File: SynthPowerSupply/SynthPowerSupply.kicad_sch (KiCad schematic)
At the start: 24 parts, among them J1 Barrel_Jack_Switch, U1 LM7812_TO220, U2 LM7912_TO220, U5 LM7805_TO220

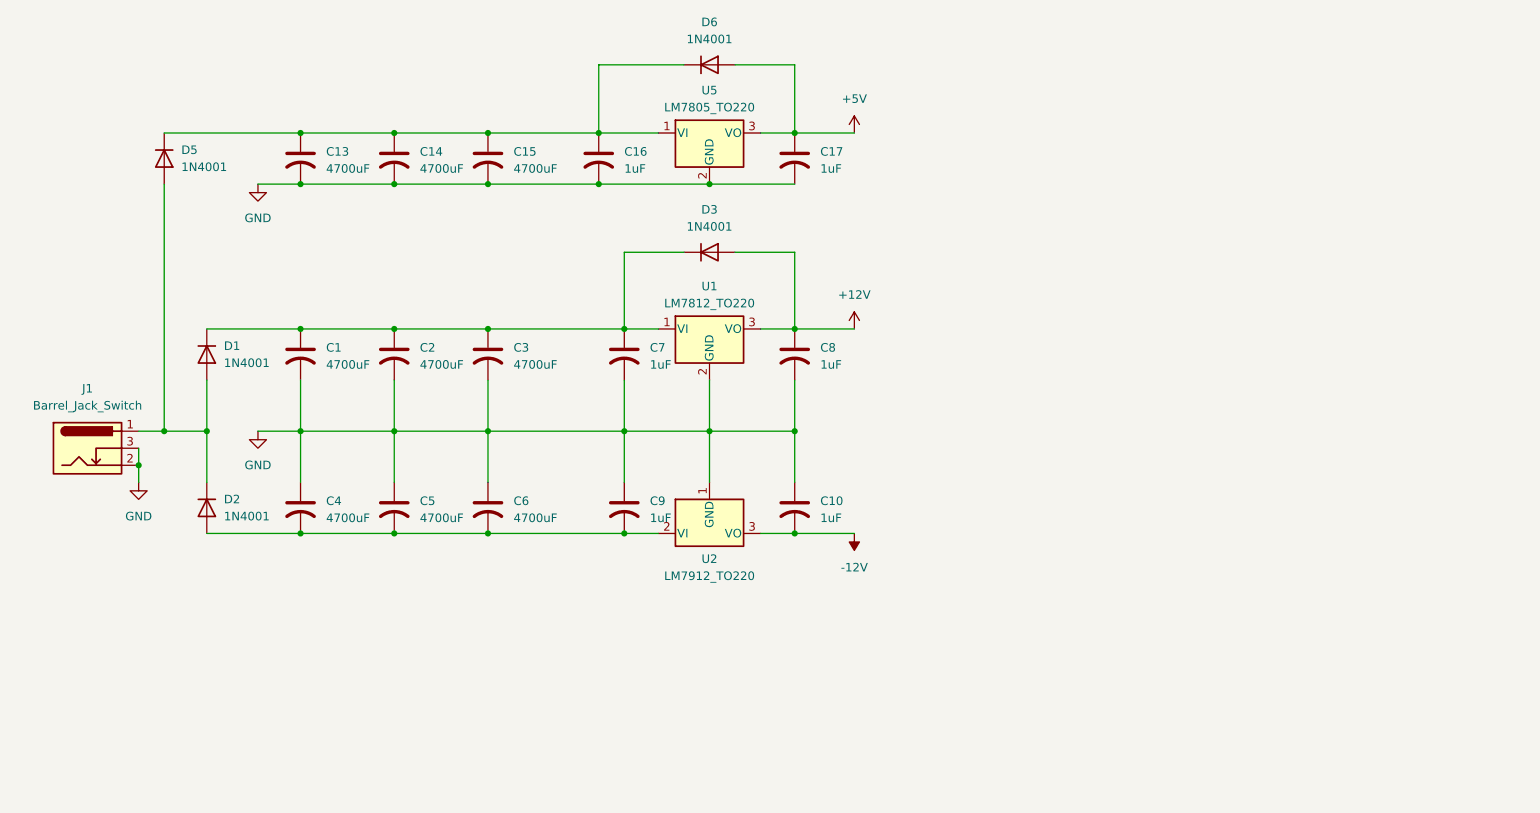
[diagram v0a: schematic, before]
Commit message: Add power schematic
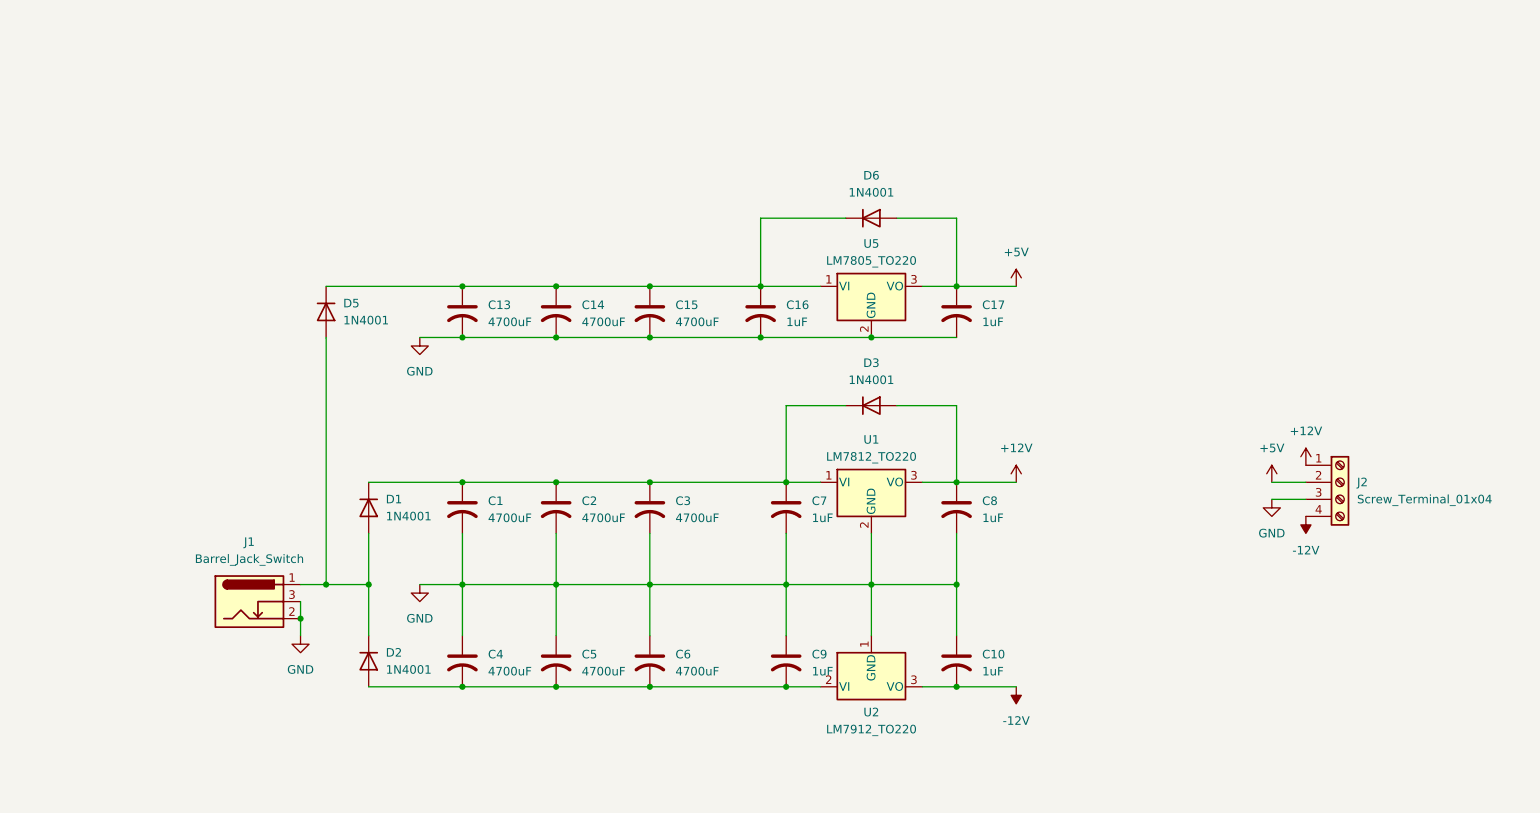
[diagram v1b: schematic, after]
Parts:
- added J2: Screw_Terminal_01x04, TerminalBlock:TerminalBlock_Xinya_XY308-2.54-4P_1x04_P2.54mm_Horizontal, symbol Connector:Screw_Terminal_01x04
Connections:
- net +12V: now also J2.1 (Pin_1)
- net +5V: now also J2.2 (Pin_2)
- net -12V: now also J2.4 (Pin_4)
- net GND: now also J2.3 (Pin_3)
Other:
- moved on the sheet: C1, C10, C13, C14, C15, C16, C17, C2, C3, C4, C5, C6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

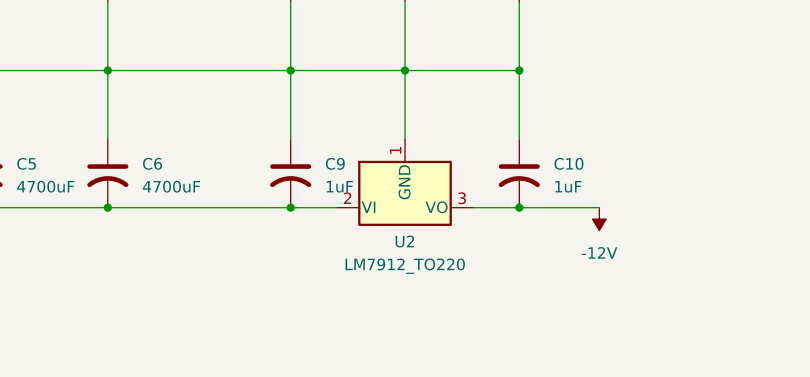
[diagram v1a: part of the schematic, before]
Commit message: Create Power supply PCB
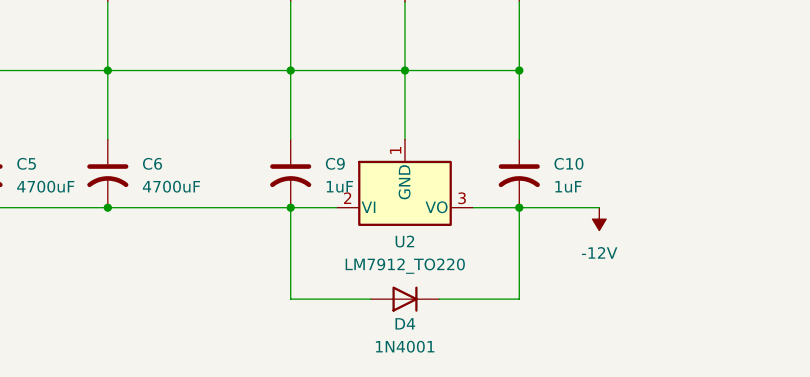
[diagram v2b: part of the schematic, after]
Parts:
- added D4: 1N4001, Diode_THT:D_DO-41_SOD81_P10.16mm_Horizontal, symbol Diode:1N4001
- C1, C13, C14, C15, C2, C3, C4, C5, C6: footprint Capacitor_THT:CP_Radial_D8.0mm_P2.50mm -> Capacitor_THT:CP_Radial_D16.0mm_P7.50mm
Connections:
- net -12V: now also D4.1 (K)
- net at C4.2, C5.2, C6.2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: now also D4.2 (A)
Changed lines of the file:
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@@
+	(wire
+		(pts
+			(xy 182.88 124.46) (xy 182.88 114.3)
+		)
+		(stroke
+			(width 0)
+			(type default)
+		)
+	)
 	(wire
 		(pts
@@
 	(wire
 		(pts
+			(xy 157.48 124.46) (xy 157.48 114.3)
+		)
+		(stroke
+			(width 0)
+			(type default)
+		)
+	)
+	(wire
+		(pts
 			(xy 137.16 99.06) (xy 137.16 106.68)
 		)
@@
 	(wire
 		(pts
+			(xy 173.99 124.46) (xy 182.88 124.46)
+		)
+		(stroke
+			(width 0)
+			(type default)
+		)
+	)
+	(wire
+		(pts
 			(xy 88.9 54.61) (xy 109.22 54.61)
 		)
@@
 		(pts
 			(xy 85.09 106.68) (xy 85.09 104.14)
+		)
+		(stroke
+			(width 0)
+			(type default)
+		)
+	)
+	(wire
+		(pts
+			(xy 166.37 124.46) (xy 157.48 124.46)
 		)
 		(stroke
@@
 			)
 		)
-		(property "Footprint" "Capacitor_THT:CP_Radial_D8.0mm_P2.50mm"
+		(property "Footprint" "Capacitor_THT:CP_Radial_D16.0mm_P7.50mm"
 			(at 137.16 110.49 0)
 			(effects
@@
 			)
 		)
-		(property "Footprint" "Capacitor_THT:CP_Radial_D8.0mm_P2.50mm"
+		(property "Footprint" "Capacitor_THT:CP_Radial_D16.0mm_P7.50mm"
 			(at 137.16 87.63 0)
 			(effects
@@
 	)
 	(symbol
+		(lib_id "Diode:1N4001")
+		(at 170.18 124.46 180)
+		(unit 1)
+		(exclude_from_sim no)
+		(in_bom yes)
+		(on_board yes)
+		(dnp no)
+		(property "Reference" "D4"
+			(at 170.18 127.254 0)
+			(effects
+				(font
+					(size 1.27 1.27)
+				)
+			)
+		)
+		(property "Value" "1N4001"
+			(at 170.18 129.794 0)
+			(effects
+				(font
+					(size 1.27 1.27)
+				)
+			)
+		)
+		(property "Footprint" "Diode_THT:D_DO-41_SOD81_P10.16mm_Horizontal"
+			(at 170.18 124.46 0)
+			(effects
+				(font
+					(size 1.27 1.27)
+				)
+				(hide yes)
+			)
+		)
+		(property "Datasheet" "http://www.vishay.com/docs/88503/1n4001.pdf"
+			(at 170.18 124.46 0)
+			(effects
+				(font
+					(size 1.27 1.27)
+				)
+				(hide yes)
+			)
+		)
+		(property "Description" "50V 1A General Purpose Rectifier Diode, DO-41"
+			(at 170.18 124.46 0)
+			(effects
+				(font
+					(size 1.27 1.27)
+				)
+				(hide yes)
+			)
+		)
+		(property "Sim.Device" "D"
+			(at 170.18 124.46 0)
+			(effects
+				(font
+					(size 1.27 1.27)
+				)
+				(hide yes)
+			)
+		)
+		(property "Sim.Pins" "1=K 2=A"
+			(at 170.18 124.46 0)
+			(effects
+				(font
+					(size 1.27 1.27)
+				)
+				(hide yes)
+			)
+		)
+		(pin "1"
+		)
+		(pin "2"
+		)
+		(instances
+			(project "SynthPowerSupply"
+				(path "/363663a4-7dd0-4c73-a57a-b99ce31fbb74"
+					(reference "D4")
+					(unit 1)
+				)
+			)
+		)
+	)
+	(symbol
 		(lib_id "Device:C_US")
 		(at 157.48 87.63 0)
@@
 			)
 		)
-		(property "Footprint" "Capacitor_THT:CP_Radial_D8.0mm_P2.50mm"
+		(property "Footprint" "Capacitor_THT:CP_Radial_D16.0mm_P7.50mm"
 			(at 123.19 58.42 0)
 			(effects
@@
 			)
 		)
-		(property "Footprint" "Capacitor_THT:CP_Radial_D8.0mm_P2.50mm"
+		(property "Footprint" "Capacitor_THT:CP_Radial_D16.0mm_P7.50mm"
 			(at 123.19 110.49 0)
 			(effects
@@
 			)
 		)
-		(property "Footprint" "Capacitor_THT:CP_Radial_D8.0mm_P2.50mm"
+		(property "Footprint" "Capacitor_THT:CP_Radial_D16.0mm_P7.50mm"
 			(at 109.22 87.63 0)
 			(effects
@@
 			)
 		)
-		(property "Footprint" "Capacitor_THT:CP_Radial_D8.0mm_P2.50mm"
+		(property "Footprint" "Capacitor_THT:CP_Radial_D16.0mm_P7.50mm"
 			(at 123.19 87.63 0)
 			(effects
@@
 			)
 		)
-		(property "Footprint" "Capacitor_THT:CP_Radial_D8.0mm_P2.50mm"
+		(property "Footprint" "Capacitor_THT:CP_Radial_D16.0mm_P7.50mm"
 			(at 137.16 58.42 0)
 			(effects
@@
 			)
 		)
-		(property "Footprint" "Capacitor_THT:CP_Radial_D8.0mm_P2.50mm"
+		(property "Footprint" "Capacitor_THT:CP_Radial_D16.0mm_P7.50mm"
 			(at 109.22 110.49 0)
 			(effects
@@
 			)
 		)
-		(property "Footprint" "Capacitor_THT:CP_Radial_D8.0mm_P2.50mm"
+		(property "Footprint" "Capacitor_THT:CP_Radial_D16.0mm_P7.50mm"
 			(at 109.22 58.42 0)
 			(effects
